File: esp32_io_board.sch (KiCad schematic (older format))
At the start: 49 parts

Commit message: schematic
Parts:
- removed JP? (x8): Jumper_3_Bridged12, symbol Jumper:Jumper_3_Bridged12
- removed R? (x2): R, symbol Device:R
- added C?: C0.1uf, symbol Device:C
- added C? (x2): 10uf, symbol Device:CP1
- added J? (x2): Conn_01x02, symbol Connector_Generic:Conn_01x02
- added J? (x8): Conn_01x03, symbol Connector_Generic:Conn_01x03
- added R? (x2): R, symbol Device:R
- added R?: R10K, symbol Device:R
- added SW?: Bootloader, symbol Switch:SW_Push
- added SW?: Reset, symbol Switch:SW_Push
- added U?: LM1117-3.3, symbol Regulator_Linear:LM1117-3.3
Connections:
- net labels added: +5V, SX00_ADDR0, SX00_ADDR1, SX01_A0, SX01_A1, SX01_A2, SX01_A3, SX01_A4, SX01_A5, SX01_A6, SX01_A7, SX01_ADDR0, SX01_ADDR1, SX01_B0, SX01_B1, SX01_B2, SX01_B3, SX01_B4, SX01_B5, SX01_B6, SX01_B7, SX02_A0, SX02_A1, SX02_A2, SX02_A3, SX02_A4, SX02_A5, SX02_A6, SX02_A7, SX02_B0, SX02_B1, SX02_B2, SX02_B3, SX02_B4, SX02_B5, SX02_B6, SX02_B7, SX03_A0, SX03_A1, SX03_A2, SX03_A3, SX03_A4, SX03_A5, SX03_A6, SX03_A7, SX03_B0, SX03_B1, SX03_B2, SX03_B3, SX03_B4, SX03_B5, SX03_B6, SX03_B7, VCC
- wire segments 253 -> 274
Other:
- moved on the sheet: D?, J?, R?, U?

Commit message: usb bus cp1202n
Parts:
- removed J?: Conn_01x02, symbol Connector_Generic:Conn_01x02
- added C? (x2): 0.01uF 16V, symbol Device:C_Small
- added C?: 4.7uF 6.3V, symbol Device:C_Small
- added D? (x2): LED, symbol Device:LED
- added D? (x2): D_TVS, symbol Device:D_TVS
- added F?: mf-msmf050-2, symbol Device:Polyfuse_Small
- added J?: USB_B_Micro, symbol Connector:USB_B_Micro
- added R? (x3): 1K, symbol Device:R
- added R? (x2): 65, symbol Device:R
- added U?: CP2102N-A01-GQFN24, Package_DFN_QFN:QFN-24-1EP_4x4mm_P0.5mm_EP2.6x2.6mm, symbol Interface_USB:CP2102N-A01-GQFN24
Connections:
- net labels added: RESET, rxd0, txd0
- net labels removed: SCL_CHB, SDA_CHB, serial_gnd, serial_rxd, serial_txd
- wire segments 274 -> 322
- no-connect marks 8 -> 19
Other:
- moved on the sheet: D?, J?, R?

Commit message: removed 3 sx1509 chips
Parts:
- removed D? (x3): LED, symbol Device:LED
- removed J? (x12): Conn_01x04, symbol Connector_Generic:Conn_01x04
- removed J? (x6): Conn_01x03, symbol Connector_Generic:Conn_01x03
- removed R? (x12): R, symbol Device:R
- removed U? (x3): SX1509, QFN-28, symbol SparkFun-DigitalIC:SX1509
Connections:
- net labels removed: ADDR0, ADDR1, SX01_A0, SX01_A1, SX01_A2, SX01_A3, SX01_A4, SX01_A5, SX01_A6, SX01_A7, SX01_ADDR0, SX01_ADDR1, SX01_B0, SX01_B1, SX01_B2, SX01_B3, SX01_B4, SX01_B5, SX01_B6, SX01_B7, SX02_A0, SX02_A1, SX02_A2, SX02_A3, SX02_A4, SX02_A5, SX02_A6, SX02_A7, SX02_B0, SX02_B1, SX02_B2, SX02_B3, SX02_B4, SX02_B5, SX02_B6, SX02_B7, SX03_A0, SX03_A1, SX03_A2, SX03_A3, SX03_A4, SX03_A5, SX03_A6, SX03_A7, SX03_B0, SX03_B1, SX03_B2, SX03_B3, SX03_B4, SX03_B5, SX03_B6, SX03_B7
- wire segments 322 -> 138
- no-connect marks 19 -> 13
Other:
- moved on the sheet: D?, J?, R?

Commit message: modified design
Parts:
- removed D?: LED, symbol Device:LED
- removed J? (x4): Conn_01x04, symbol Connector_Generic:Conn_01x04
- removed J? (x2): Conn_01x03, symbol Connector_Generic:Conn_01x03
- removed R? (x4): R, symbol Device:R
- removed U?: SX1509, QFN-28, symbol SparkFun-DigitalIC:SX1509
- added J?: Conn_02x04_Counter_Clockwise, symbol Connector_Generic:Conn_02x04_Counter_Clockwise
- added J? (x2): Conn_01x02, symbol Connector_Generic:Conn_01x02
- added U? (x2): TXB0104PW, Package_SO:TSSOP-14_4.4x5mm_P0.65mm, symbol Logic_LevelTranslator:TXB0104PW
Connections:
- net labels added: pin10, pin11, pin12, pin13, pin6, pin7, pin8, pin9
- net labels removed: SCL_CHA, SDA_CHA, SX00_A0, SX00_A1, SX00_A2, SX00_A3, SX00_A4, SX00_A5, SX00_A6, SX00_A7, SX00_ADDR0, SX00_ADDR1, SX00_B0, SX00_B1, SX00_B2, SX00_B3, SX00_B4, SX00_B5, SX00_B6, SX00_B7
- wire segments 138 -> 118
- no-connect marks 13 -> 12

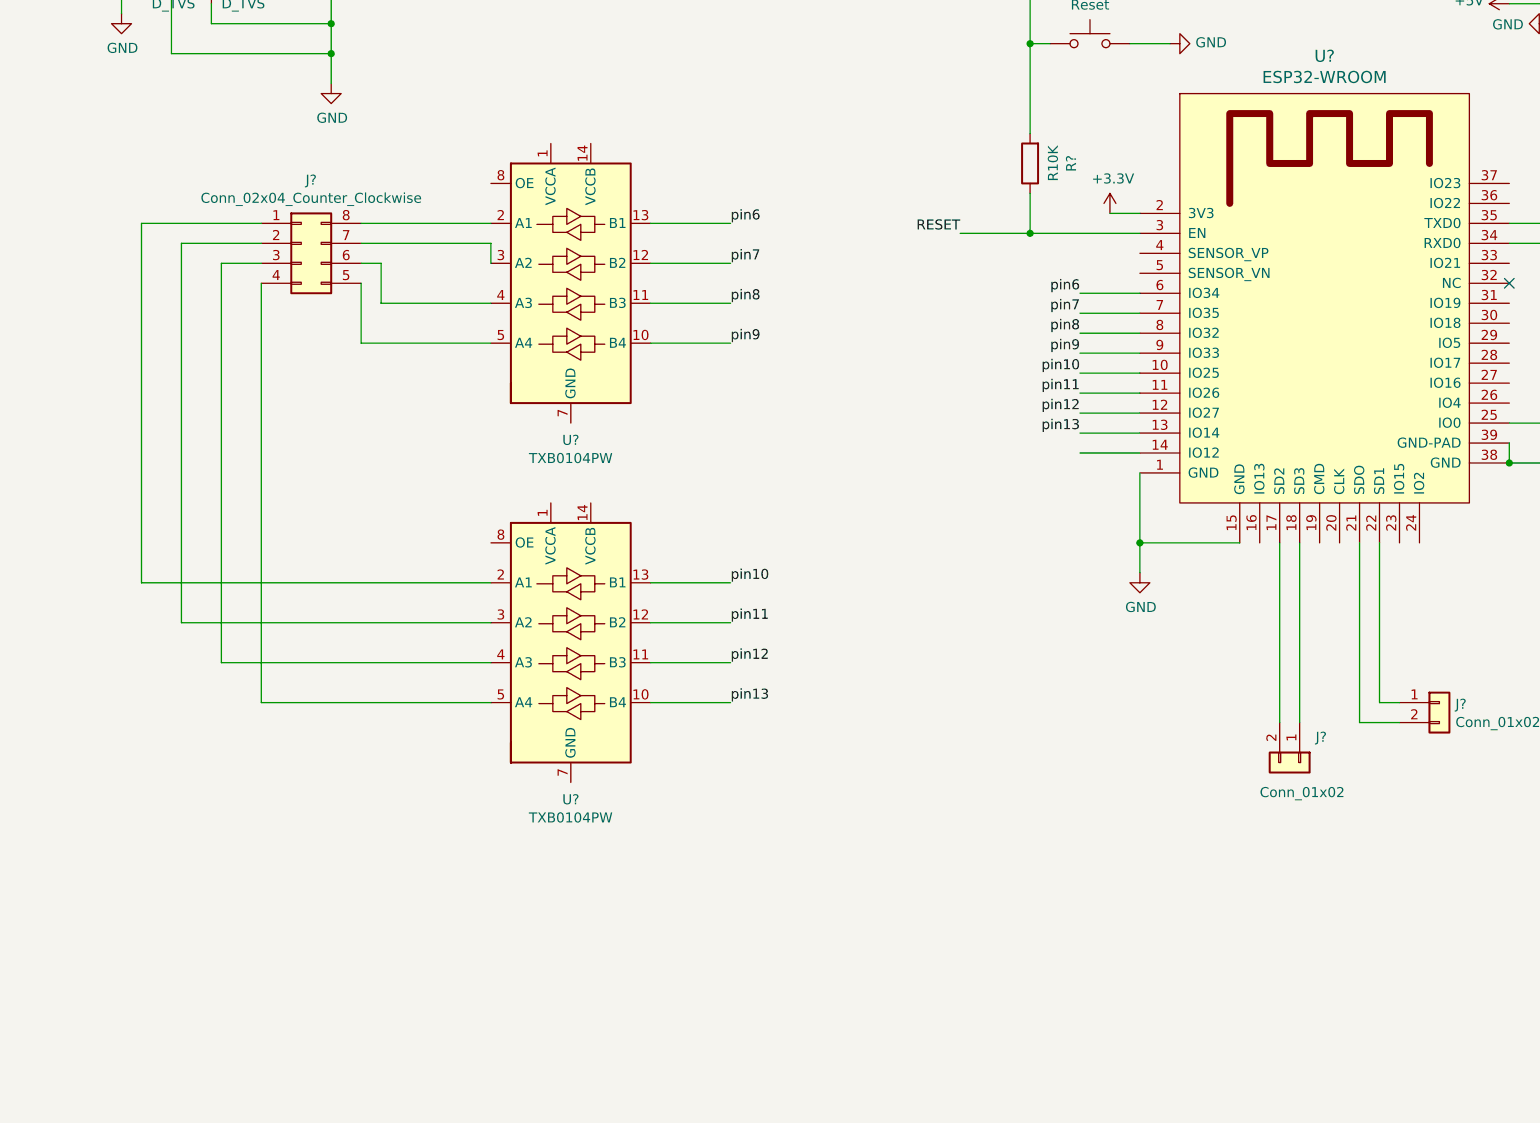
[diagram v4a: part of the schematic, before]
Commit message: rgb addressable led indication
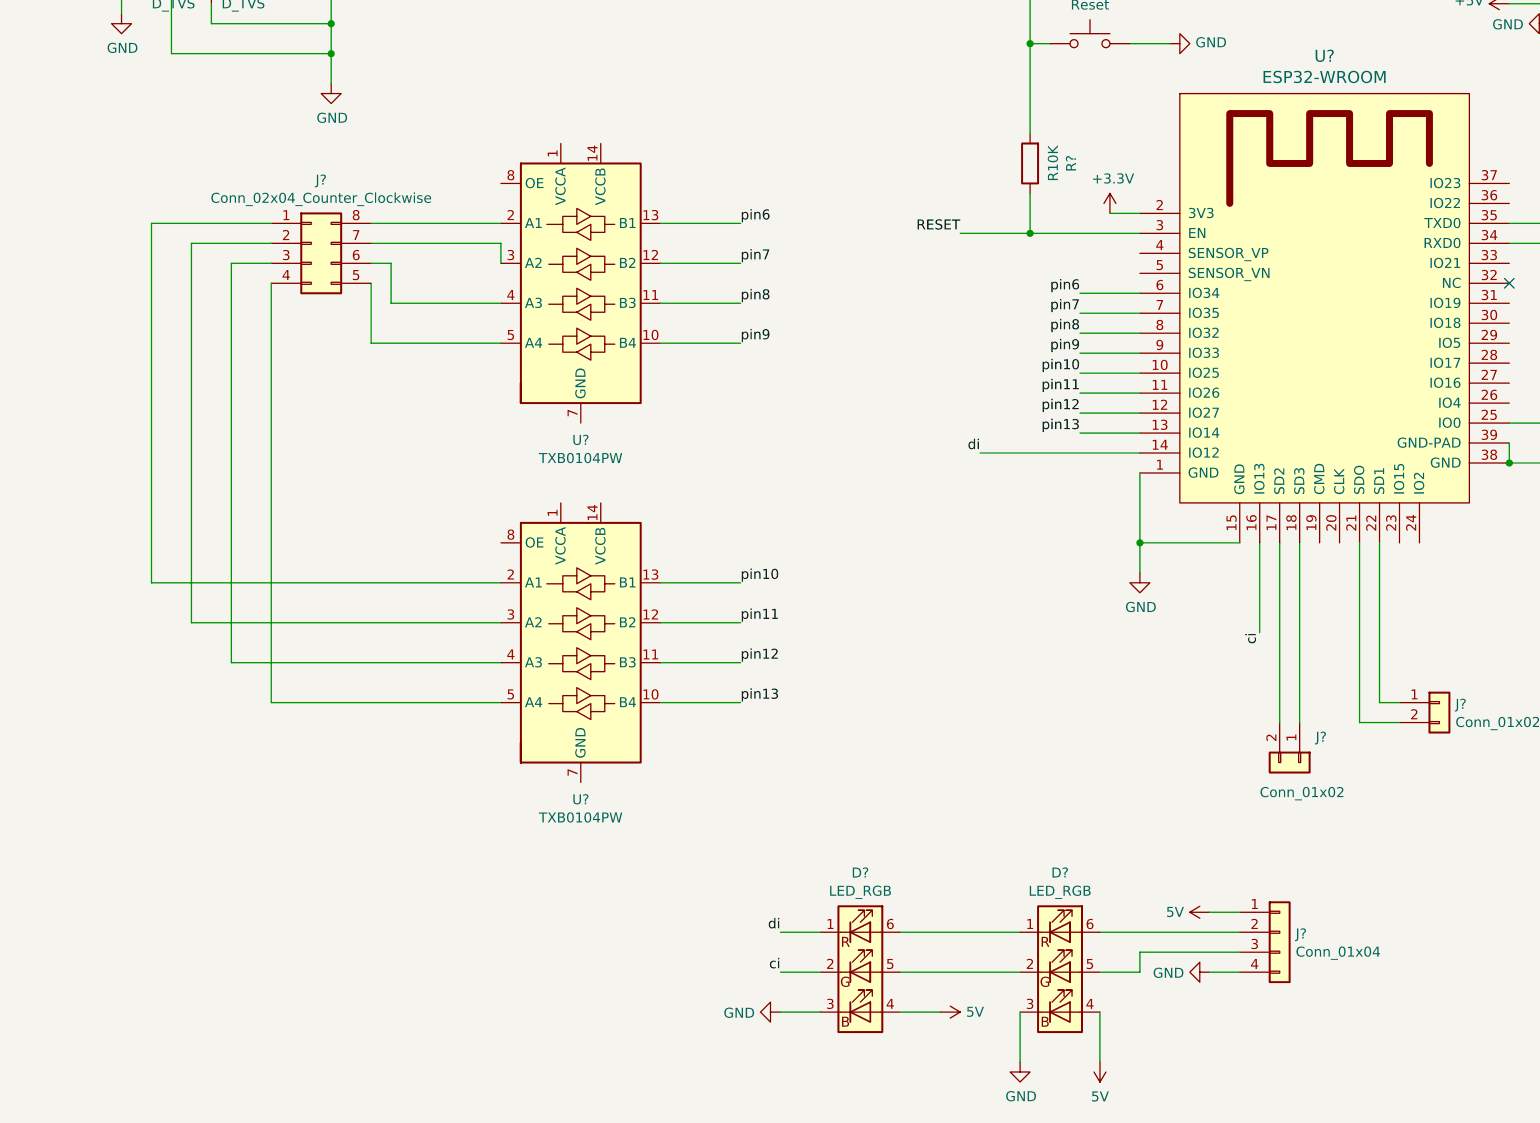
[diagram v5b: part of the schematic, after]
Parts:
- added D? (x2): LED_RGB, symbol Device:LED_RGB
- added J?: Conn_01x04, symbol Connector_Generic:Conn_01x04
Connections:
- net GND: now also D?.3 (BK), D?.3 (BK), J?.4 (Pin_4)
- net di: now reaches U?.14 (IO12)
- net di: now also D?.1 (RK)
- net ci: now reaches U?.16 (IO13)
- net ci: now also D?.2 (GK)
- new net: D?.2 (GK), D?.5 (GA)
- new net: D?.1 (RK), D?.6 (RA)
- new net: D?.5 (GA), J?.3 (Pin_3)
- new net: D?.6 (RA), J?.2 (Pin_2)
- new net 5V: D?.4 (BA), D?.4 (BA), J?.1 (Pin_1)
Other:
- moved on the sheet: J?, U?

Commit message: tca9548
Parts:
- added C?: C_Small, symbol Device:C_Small
- added J? (x8): Conn_01x02, symbol Connector_Generic:Conn_01x02
- added JP? (x3): SolderJumper_2_Open, symbol Jumper:SolderJumper_2_Open
- added R? (x4): R_Small, symbol Device:R_Small
- added U?: TCA9548APWR, Package_SO:TSSOP-24_4.4x7.8mm_P0.65mm, symbol Interface_Expansion:TCA9548APWR
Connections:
- net 5V is gone; now on net +5V: D?.4 (BA), D?.4 (BA), J?.1 (Pin_1)
- net +3V3: now also C?.1, JP?.2 (B), JP?.2 (B), JP?.2 (B), R?.2, U?.24 (VCC)
- net GND: now also C?.2, R?.2, R?.2, R?.2, U?.12 (GND)
- net at U?.21 (SDO): now also U?.23 (SDA); no longer J?.2 (Pin_2)
- net at U?.22 (SD1): now also U?.22 (SCL); no longer J?.1 (Pin_1)
- new net: JP?.1 (A), R?.1, U?.1 (A0)
- new net: J?.2 (Pin_2), U?.10 (SD3)
- new net: J?.1 (Pin_1), U?.11 (SC3)
- new net: J?.2 (Pin_2), U?.13 (SD4)
- new net: J?.1 (Pin_1), U?.14 (SC4)
- new net: J?.2 (Pin_2), U?.15 (SD5)
- new net: J?.1 (Pin_1), U?.16 (SC5)
- new net: J?.2 (Pin_2), U?.17 (SD6)
- new net: J?.1 (Pin_1), U?.18 (SC6)
- new net: J?.2 (Pin_2), U?.19 (SD7)
- new net: JP?.1 (A), R?.1, U?.2 (A1)
- new net: J?.1 (Pin_1), U?.20 (SC7)
- new net: JP?.1 (A), R?.1, U?.21 (A2)
- new net: R?.1, U?.3 (~RESET)
- new net: J?.2 (Pin_2), U?.4 (SD0)
- new net: J?.1 (Pin_1), U?.5 (SC0)
- new net: J?.2 (Pin_2), U?.6 (SD1)
- new net: J?.1 (Pin_1), U?.7 (SC1)
- new net: J?.2 (Pin_2), U?.8 (SD2)
- new net: J?.1 (Pin_1), U?.9 (SC2)
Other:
- moved on the sheet: D?, J?

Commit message: spi ports
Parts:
- added J?: Conn_01x02, symbol Connector_Generic:Conn_01x02
- added J?: Conn_02x04_Counter_Clockwise, symbol Connector_Generic:Conn_02x04_Counter_Clockwise
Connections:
- net +3V3: now also J?.5 (Pin_5), J?.6 (Pin_6)
- net GND: now also J?.7 (Pin_7), J?.8 (Pin_8)
- net at U?.29 (IO5): now also J?.4 (Pin_4)
- net at U?.30 (IO18): now also J?.3 (Pin_3)
- net at U?.31 (IO19): now also J?.2 (Pin_2)
- net at U?.37 (IO23): now also J?.1 (Pin_1)
- net at U?.4 (SENSOR_VP): now also J?.2 (Pin_2)
- net at U?.5 (SENSOR_VN): now also J?.1 (Pin_1)
- no-connect marks 12 -> 13
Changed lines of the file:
@@
 Wire Wire Line
 	12300 9250 12550 9250
+Wire Wire Line
+	9150 5500 8250 5500
+Wire Wire Line
+	9150 5600 8250 5600
+$Comp
+L Connector_Generic:Conn_01x02 J?
+U 1 1 5C5C727F
+P 8050 5600
+F 0 "J?" H 8130 5592 50  0000 L CNN
+F 1 "Conn_01x02" H 8130 5501 50  0000 L CNN
+F 2 "" H 8050 5600 50  0001 C CNN
+F 3 "~" H 8050 5600 50  0001 C CNN
+	1    8050 5600
+	-1   0    0    1
+$EndComp
+NoConn ~ 10150 6950
+$Comp
+L Connector_Generic:Conn_02x04_Counter_Clockwise J?
+U 1 1 5C5FA466
+P 12400 5750
+F 0 "J?" H 12450 6067 50  0000 C CNN
+F 1 "Conn_02x04_Counter_Clockwise" H 12450 5976 50  0000 C CNN
+F 2 "" H 12400 5750 50  0001 C CNN
+F 3 "~" H 12400 5750 50  0001 C CNN
+	1    12400 5750
+	1    0    0    -1
+$EndComp
+Wire Wire Line
+	12200 5750 11000 5750
+Wire Wire Line
+	12200 5850 11000 5850
+Wire Wire Line
+	11000 5950 12200 5950
+Wire Wire Line
+	11000 5150 12200 5150
+Wire Wire Line
+	12200 5150 12200 5650
+Wire Wire Line
+	12700 5850 12700 5950
+Connection ~ 12700 5950
+Wire Wire Line
+	12700 5950 12700 6100
+Wire Wire Line
+	12700 5750 12700 5650
+Connection ~ 12700 5650
+Wire Wire Line
+	12700 5500 12700 5650
+$Comp
+L power:+3.3V #PWR?
+U 1 1 5C6D291C
+P 12700 6100
+F 0 "#PWR?" H 12700 5950 50  0001 C CNN
+F 1 "+3.3V" H 12715 6273 50  0000 C CNN
+F 2 "" H 12700 6100 50  0001 C CNN
+F 3 "" H 12700 6100 50  0001 C CNN
+	1    12700 6100
+	-1   0    0    1
+$EndComp
+$Comp
+L power:GND #PWR?
+U 1 1 5C6E6494
+P 12700 5500
+F 0 "#PWR?" H 12700 5250 50  0001 C CNN
+F 1 "GND" V 12705 5372 50  0000 R CNN
+F 2 "" H 12700 5500 50  0001 C CNN
+F 3 "" H 12700 5500 50  0001 C CNN
+	1    12700 5500
+	-1   0    0    1
+$EndComp
 $EndSCHEMATC

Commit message: final schematic
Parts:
- added C? (x4): C_Small, symbol Device:C_Small
- added D?: LED, symbol Device:LED
- added J? (x2): Conn_01x02, symbol Connector_Generic:Conn_01x02
- added R?: R_Small, symbol Device:R_Small
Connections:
- net +3V3: now also U?.14 (VCCB), C?.2
- net +5V: now also U?.1 (VCCA), C?.1, C?.2
- net GND: now also U?.7 (GND), U?.7 (GND), C?.1, C?.1, C?.2, C?.2, D?.1 (K)
- net at U?.23 (IO15): now also J?.2 (Pin_2)
- net at U?.24 (IO2): now also J?.1 (Pin_1)
- net at U?.26 (IO4): now also R?.2
- net at U?.27 (IO16): now also J?.2 (Pin_2)
- net at U?.28 (IO17): now also J?.1 (Pin_1)
- net at U?.33 (IO21): now also J?.2 (Pin_2)
- net at U?.36 (IO22): now also J?.1 (Pin_1)
- new net: D?.2 (A), R?.1
- new net 3.3V: C?.1
- no-connect marks 13 -> 14
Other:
- moved on the sheet: J?
